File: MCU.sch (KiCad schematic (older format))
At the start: 119 parts, among them P801 JTAG, Q201 BC817-40, U201 STM32F439NIH6, Y201 32kHz, Y202 24MHz

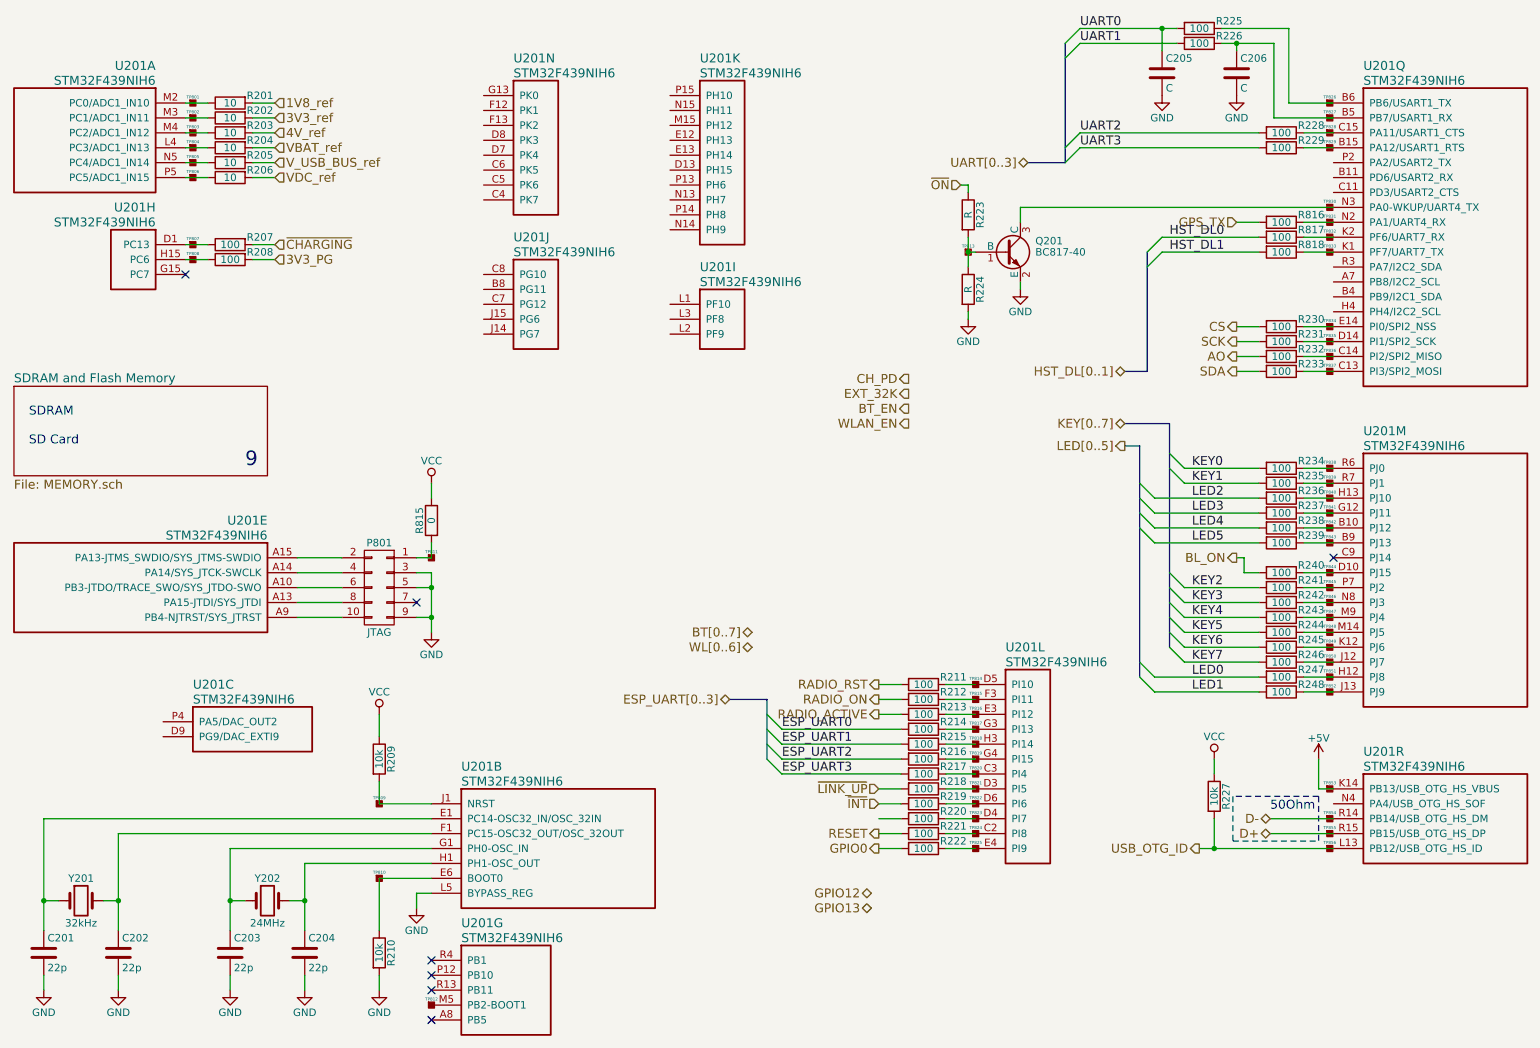
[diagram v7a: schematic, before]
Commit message: Added Interface for OLED display
Added Booster for 4V -> 15V
Added bus for display data
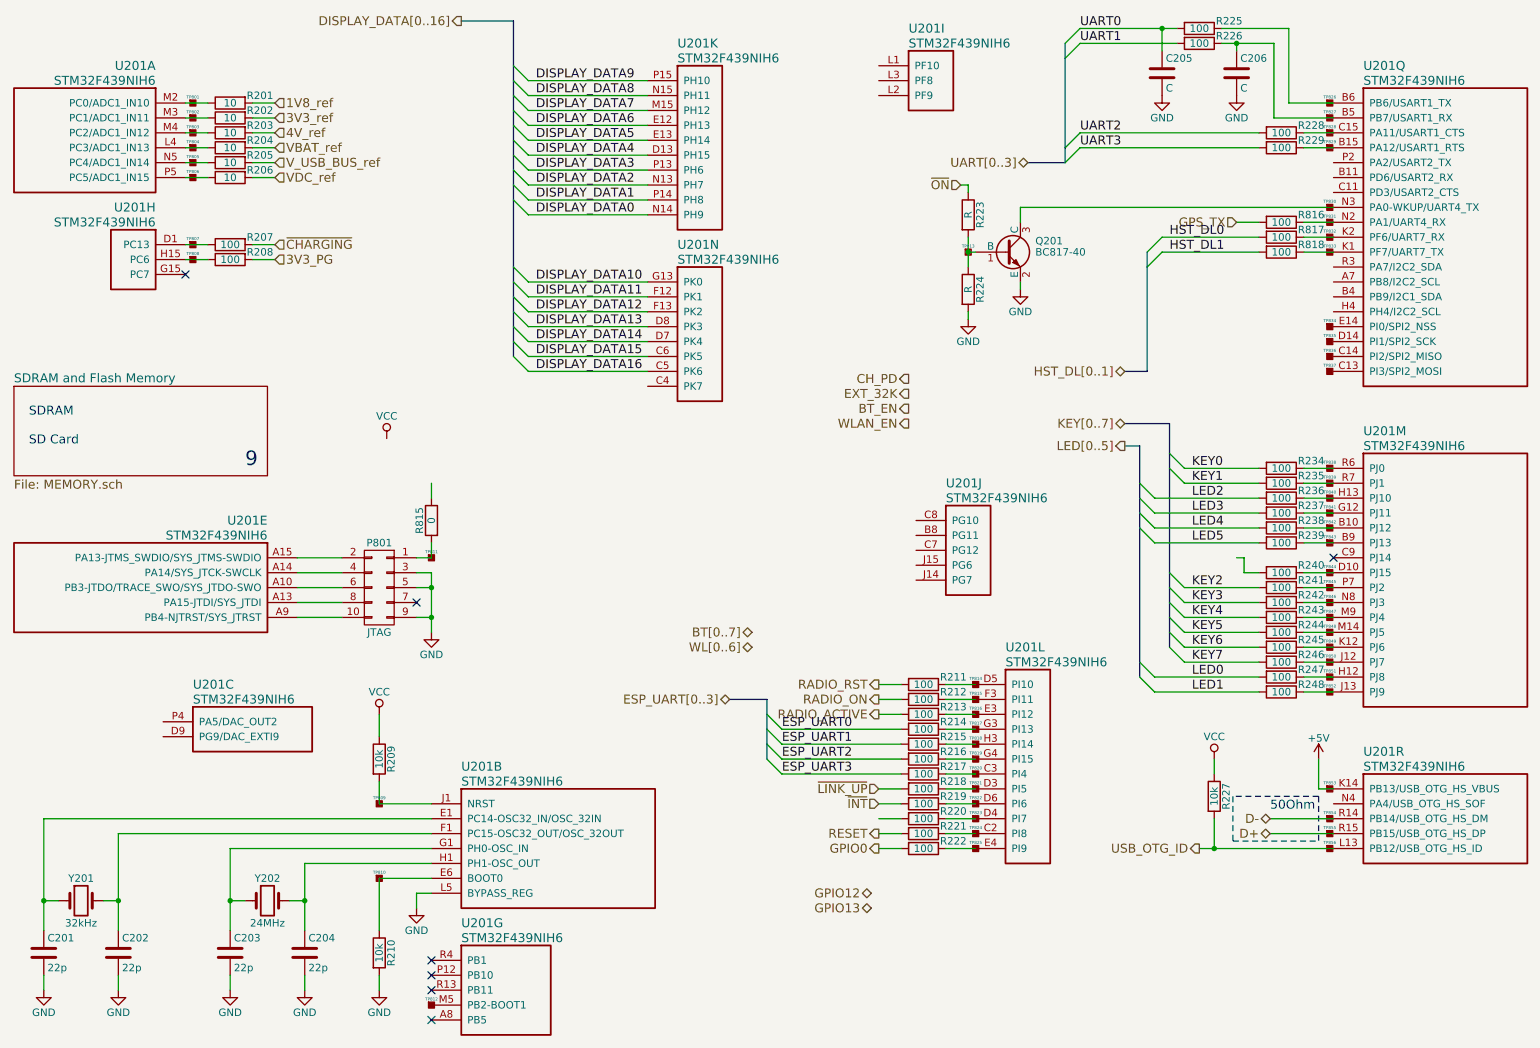
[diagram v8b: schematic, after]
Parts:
- removed R230, R231, R232, R233: 100, Resistors_SMD:R_0603, symbol R
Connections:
- net VCC: no longer R815.1
- net DISPLAY_DATA4: now reaches U201.D13 (PH15)
- net DISPLAY_DATA6: now reaches U201.E12 (PH13)
- net DISPLAY_DATA5: now reaches U201.E13 (PH14)
- net DISPLAY_DATA7: now reaches U201.M15 (PH12)
- net DISPLAY_DATA2: now reaches U201.N13 (PH7)
- net DISPLAY_DATA0: now reaches U201.N14 (PH9)
- net DISPLAY_DATA8: now reaches U201.N15 (PH11)
- net DISPLAY_DATA3: now reaches U201.P13 (PH6)
- net DISPLAY_DATA1: now reaches U201.P14 (PH8)
- net DISPLAY_DATA9: now reaches U201.P15 (PH10)
- net DISPLAY_DATA16: now reaches U201.C5 (PK6)
- net DISPLAY_DATA15: now reaches U201.C6 (PK5)
- net DISPLAY_DATA14: now reaches U201.D7 (PK4)
- net DISPLAY_DATA13: now reaches U201.D8 (PK3)
- net DISPLAY_DATA11: now reaches U201.F12 (PK1)
- net DISPLAY_DATA12: now reaches U201.F13 (PK2)
- net DISPLAY_DATA10: now reaches U201.G13 (PK0)
- net BL_ON: no longer names the net of R240.2
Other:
- moved on the sheet: U201I, U201J, U201K, U201N
